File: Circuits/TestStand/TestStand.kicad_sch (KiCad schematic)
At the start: 84 parts, among them J1 Screw_Terminal_01x07, J10 Screw_Terminal_01x03, J11 Screw_Terminal_01x03, J12 Screw_Terminal_01x03, J13 Screw_Terminal_01x03, J14 Screw_Terminal_01x02, J15 Conn_Coaxial, J2 Screw_Terminal_01x07, J3 Screw_Terminal_01x07, J4 Screw_Terminal_01x03, J5 Screw_Terminal_01x03, J6 Screw_Terminal_01x03, J7 Screw_Terminal_01x03, J8 Screw_Terminal_01x03, J9 Screw_Terminal_01x03, Q1 MMBT4403-7-F, Q2 MMBT4403-7-F, Q3 MMBT4403-7-F, U1 HX711, U2 HX711, U3 HX711, U4 Teensy4.1, U5 LP2980IM5X-3.3/NOPB, U6 MAX31855KASA, U7 NRF24L01, U8 LP2980IM5X-3.3/NOPB, Y1 16Mhz

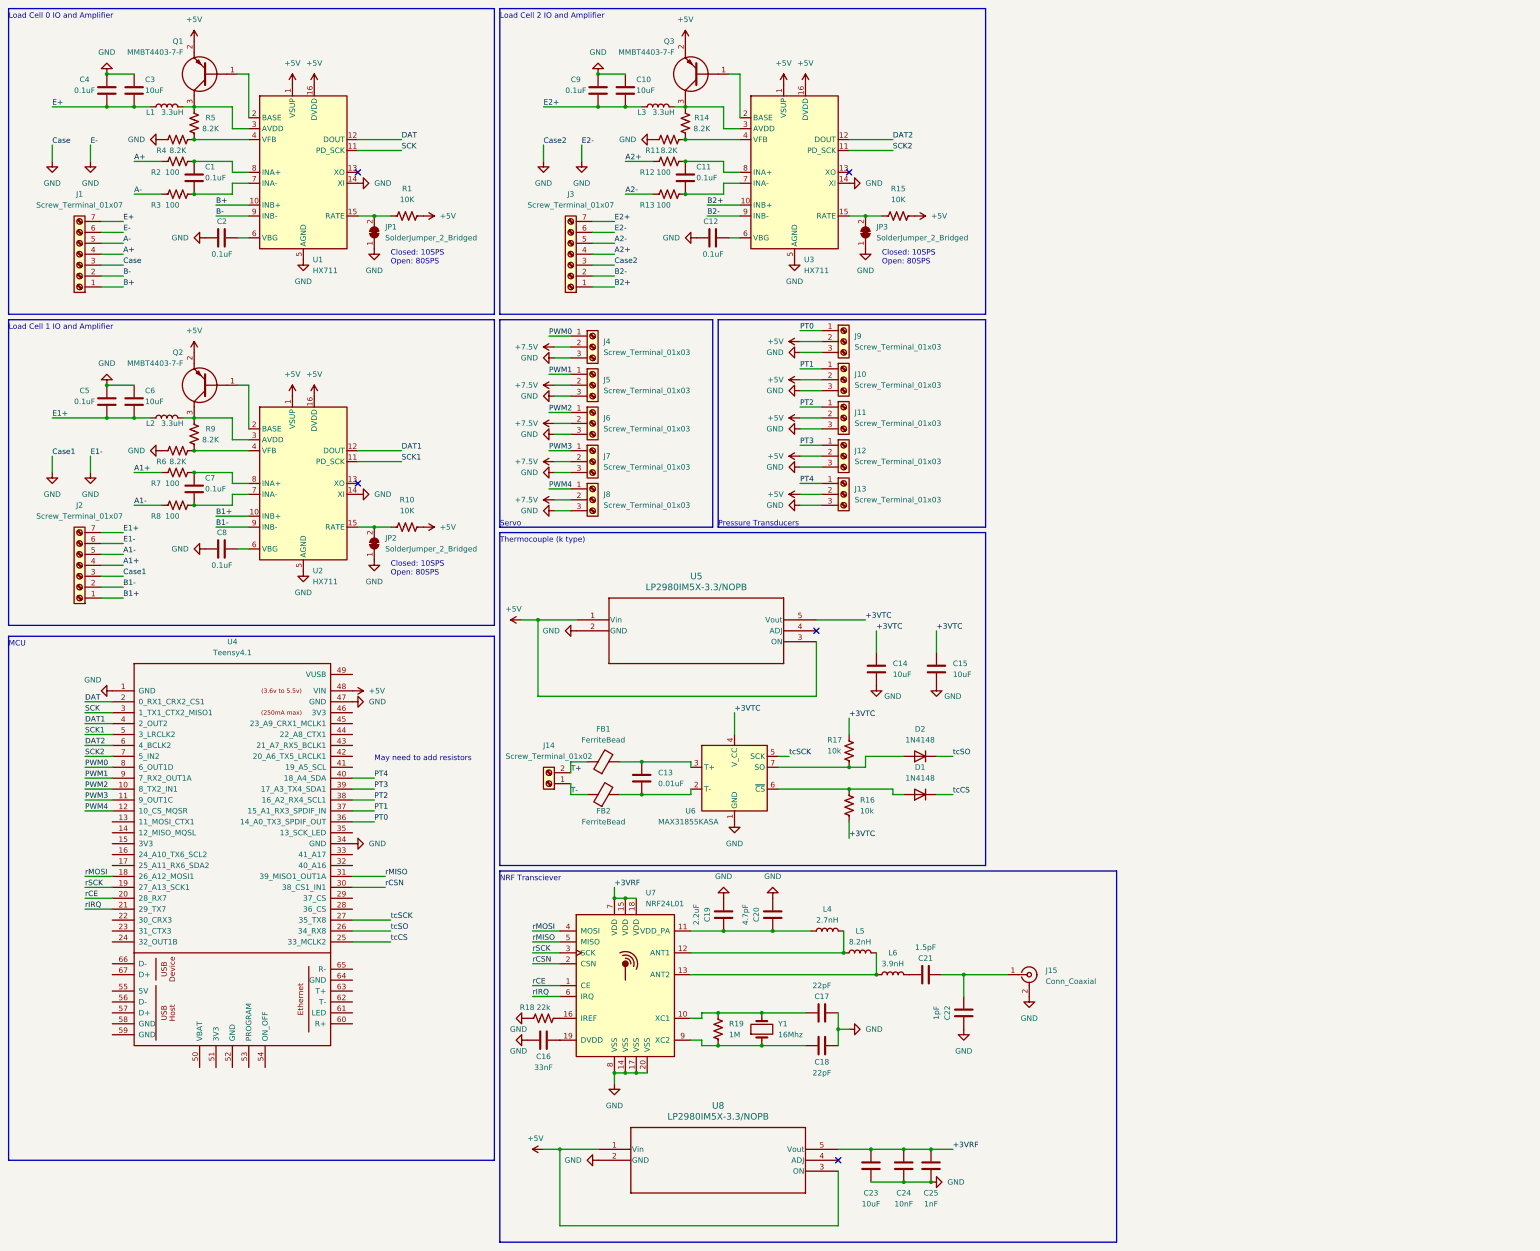
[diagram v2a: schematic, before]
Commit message: added glow plug circuitry to schematic
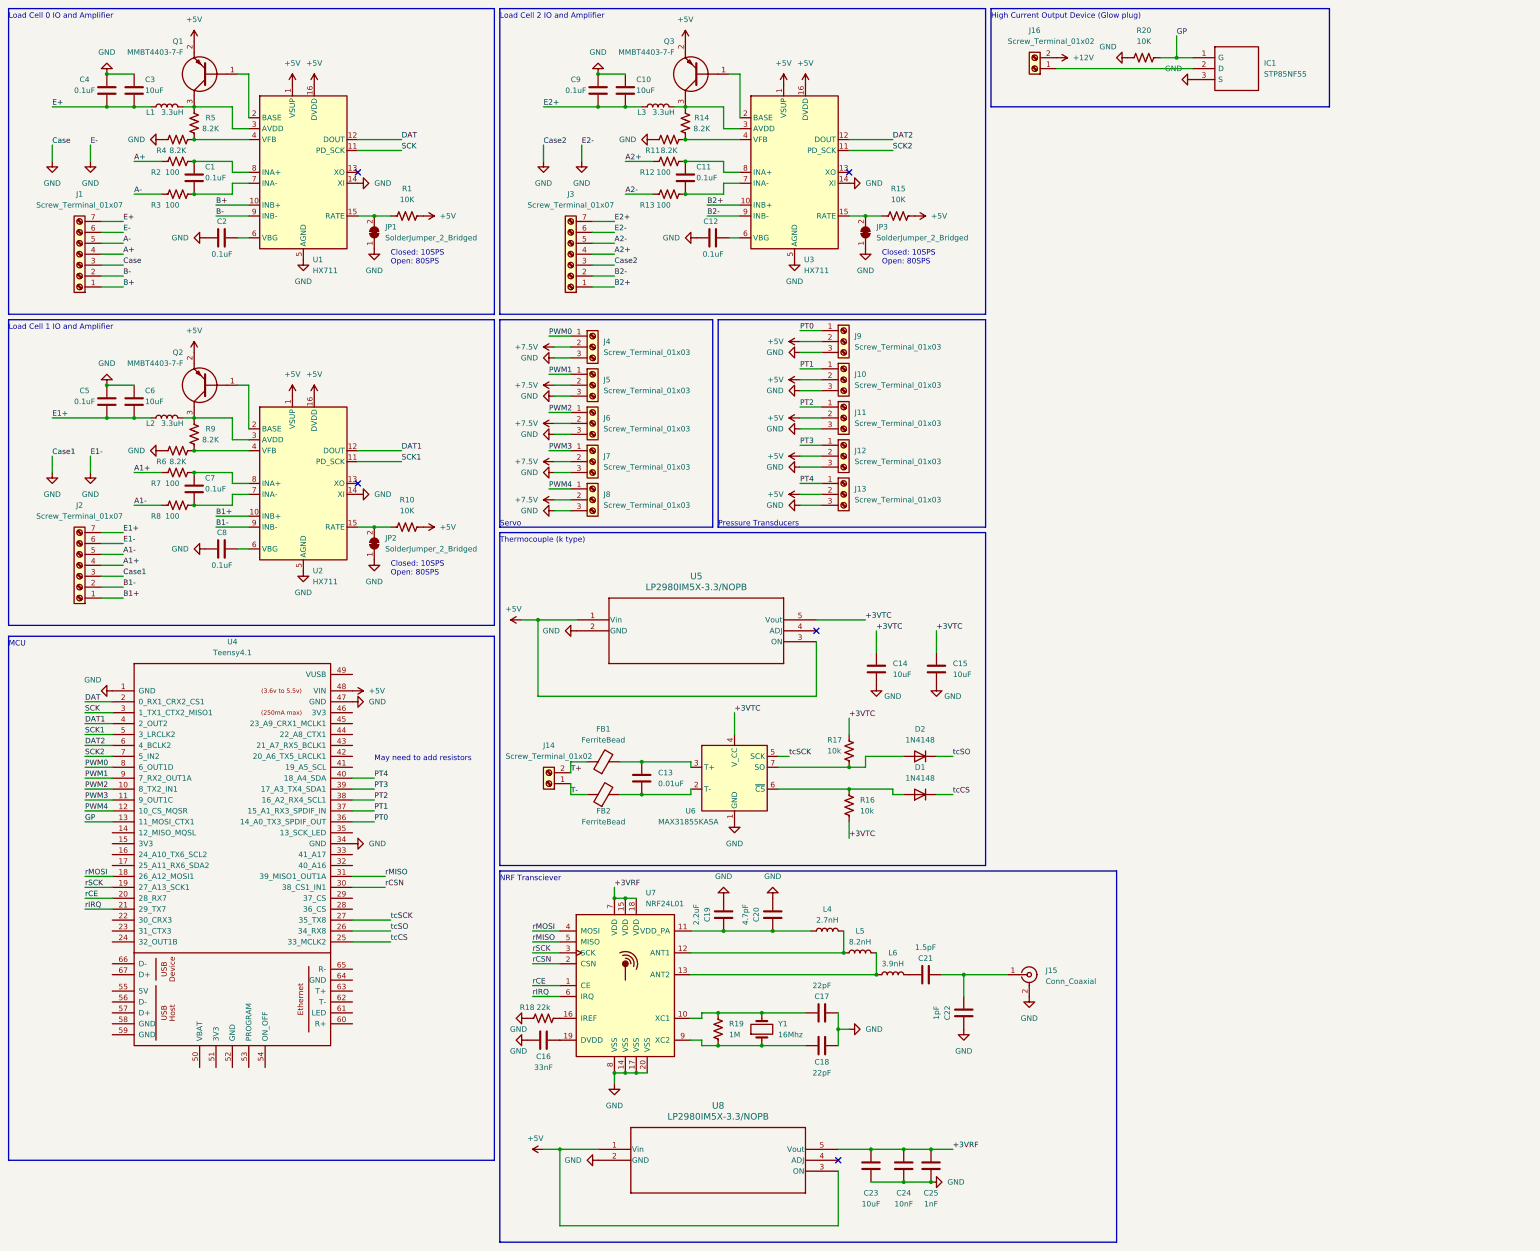
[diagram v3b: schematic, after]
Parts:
- added IC1: STP85NF55, TO255P460X1020X2008-3P, symbol STP85NF55:STP85NF55
- added J16: Screw_Terminal_01x02, Connector_Wago:Wago_734-132_1x02_P3.50mm_Vertical, symbol Connector:Screw_Terminal_01x02
- added R20: 10K, Resistor_SMD:R_0805_2012Metric, symbol Device:R_US
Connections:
- net GND: now also IC1.3 (S), R20.1
- net GP: now reaches U4.13 (11_MOSI_CTX1)
- net GP: now also IC1.1 (G), R20.2
- new net: IC1.2 (D), J16.1 (Pin_1)
- new net +12V: J16.2 (Pin_2)
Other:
- note added: "High Current Output Device (Glow plug)"
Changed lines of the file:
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@@
   (junction (at 59.69 133.35) (diameter 0) (color 0 0 0 0)
   )
+  (junction (at 288.29 29.21) (diameter 0) (color 0 0 0 0)
+  )
   (junction (at 153.67 33.02) (diameter 0) (color 0 0 0 0)
   )
@@
     (stroke (width 0) (type default))
   )
+  (wire (pts (xy 260.35 31.75) (xy 292.1 31.75))
+    (stroke (width 0) (type default))
+  )
+  (wire (pts (xy 284.48 29.21) (xy 288.29 29.21))
+    (stroke (width 0) (type default))
+  )
   (wire (pts (xy 35.56 121.92) (xy 35.56 125.73))
     (stroke (width 0) (type default))
@@
     (stroke (width 0) (type default))
   )
+  (wire (pts (xy 288.29 24.13) (xy 288.29 29.21))
+    (stroke (width 0) (type default))
+  )
   (wire (pts (xy 157.48 265.43) (xy 160.02 265.43))
     (stroke (width 0) (type default))
@@
     (stroke (width 0) (type default))
   )
+  (wire (pts (xy 34.29 207.01) (xy 40.64 207.01))
+    (stroke (width 0) (type default))
+  )
   (wire (pts (xy 69.85 105.41) (xy 72.39 105.41))
     (stroke (width 0) (type default))
@@
     (stroke (width 0) (type default))
   )
+  (wire (pts (xy 288.29 29.21) (xy 292.1 29.21))
+    (stroke (width 0) (type default))
+  )
   (wire (pts (xy 200.66 119.38) (xy 205.74 119.38))
     (stroke (width 0) (type default))
@@
     (fill (type none))
   )
+  (rectangle (start 245.11 17.78) (end 323.85 40.64)
+    (stroke (width 0) (type default))
+    (fill (type none))
+  )
   (rectangle (start 130.81 218.44) (end 274.32 304.8)
     (stroke (width 0) (type default))
@@
     (effects (font (size 1.27 1.27)) (justify left bottom))
   )
+  (text "High Current Output Device (Glow plug)\n" (at 245.11 20.32 0)
+    (effects (font (size 1.27 1.27)) (justify left bottom))
+  )
   (text "Closed: 10SPS\nOpen: 80SPS" (at 105.41 149.86 0)
     (effects (font (size 1.27 1.27)) (justify left bottom))
@@
     (effects (font (size 1.27 1.27)) (justify left bottom))
   )
+  (label "GP" (at 34.29 207.01 0) (fields_autoplaced)
+    (effects (font (size 1.27 1.27)) (justify left bottom))
+  )
   (label "rCSN" (at 138.43 240.03 0) (fields_autoplaced)
     (effects (font (size 1.27 1.27)) (justify left bottom))
@@
     (effects (font (size 1.27 1.27)) (justify left bottom))
   )
+  (label "GP" (at 288.29 24.13 0) (fields_autoplaced)
+    (effects (font (size 1.27 1.27)) (justify left bottom))
+  )
   (label "A1-" (at 45.72 133.35 0) (fields_autoplaced)
     (effects (font (size 1.27 1.27)) (justify left bottom))
@@
     )
   )
+  (symbol (lib_id "power:GND") (at 292.1 34.29 270) (unit 1)
+    (in_bom yes) (on_board yes) (dnp no)
+    (property "Reference" "#PWR079" (at 285.75 34.29 0)
+      (effects (font (size 1.27 1.27)) hide)
+    )
+    (property "Value" "GND" (at 289.56 31.75 90)
+      (effects (font (size 1.27 1.27)) (justify right))
+    )
+    (property "Footprint" "" (at 292.1 34.29 0)
+      (effects (font (size 1.27 1.27)) hide)
+    )
+    (property "Datasheet" "" (at 292.1 34.29 0)
+      (effects (font (size 1.27 1.27)) hide)
+    )
+    (pin "1")
+    (instances
+      (project "TestStand"
+        (path "/685411e9-e044-4af3-ae59-8bb36f8f4098"
+          (reference "#PWR079") (unit 1)
+        )
+      )
+    )
+  )
   (symbol (lib_id "power:GND") (at 35.56 53.34 0) (unit 1)
     (in_bom yes) (on_board yes) (dnp no) (fields_autoplaced)
@@
     )
   )
+  (symbol (lib_id "power:+12V") (at 260.35 29.21 270) (unit 1)
+    (in_bom yes) (on_board yes) (dnp no) (fields_autoplaced)
+    (property "Reference" "#PWR077" (at 256.54 29.21 0)
+      (effects (font (size 1.27 1.27)) hide)
+    )
+    (property "Value" "+12V" (at 264.16 29.21 90)
+      (effects (font (size 1.27 1.27)) (justify left))
+    )
+    (property "Footprint" "" (at 260.35 29.21 0)
+      (effects (font (size 1.27 1.27)) hide)
+    )
+    (property "Datasheet" "" (at 260.35 29.21 0)
+      (effects (font (size 1.27 1.27)) hide)
+    )
+    (pin "1")
+    (instances
+      (project "TestStand"
+        (path "/685411e9-e044-4af3-ae59-8bb36f8f4098"
+          (reference "#PWR077") (unit 1)
+        )
+      )
+    )
+  )
   (symbol (lib_id "power:+5V") (at 82.55 107.95 0) (unit 1)
     (in_bom yes) (on_board yes) (dnp no) (fields_autoplaced)
@@
     )
   )
+  (symbol (lib_id "STP85NF55:STP85NF55") (at 292.1 29.21 0) (unit 1)
+    (in_bom yes) (on_board yes) (dnp no) (fields_autoplaced)
+    (property "Reference" "IC1" (at 308.61 30.48 0)
+      (effects (font (size 1.27 1.27)) (justify left))
+    )
+    (property "Value" "STP85NF55" (at 308.61 33.02 0)
+      (effects (font (size 1.27 1.27)) (justify left))
+    )
+    (property "Footprint" "TO255P460X1020X2008-3P" (at 308.61 26.67 0)
+      (effects (font (size 1.27 1.27)) (justify left) hide)
+    )
+    (property "Datasheet" "https://www.st.com/resource/en/datasheet/stb85nf55t4.pdf" (at 308.61 29.21 0)
+      (effects (font (size 1.27 1.27)) (justify left) hide)
+    )
+    (property "Description" "Automotive-grade N-channel 55 V, 0.0062 Ohm typ., 42 A, STripFET(TM) II Power MOSFET in TO-220 package" (at 308.61 31.75 0)
+      (effects (font (size 1.27 1.27)) (justify left) hide)
+    )
+    (property "Height" "4.6" (at 308.61 34.29 0)
+      (effects (font (size 1.27 1.27)) (justify left) hide)
+    )
+    (property "Mouser Part Number" "511-STP85NF55" (at 308.61 36.83 0)
+      (effects (font (size 1.27 1.27)) (justify left) hide)
+    )
+    (property "Mouser Price/Stock" "https://www.mouser.co.uk/ProductDetail/STMicroelectronics/STP85NF55?qs=mdiO5HdF0KgIATm5G3vEuw%3D%3D" (at 308.61 39.37 0)
+      (effects (font (size 1.27 1.27)) (justify left) hide)
+    )
+    (property "Manufacturer_Name" "STMicroelectronics" (at 308.61 41.91 0)
+      (effects (font (size 1.27 1.27)) (justify left) hide)
+    )
+    (property "Manufacturer_Part_Number" "STP85NF55" (at 308.61 44.45 0)
+      (effects (font (size 1.27 1.27)) (justify left) hide)
+    )
+    (pin "3")
+    (pin "1")
+    (pin "2")
+    (instances
+      (project "TestStand"
+        (path "/685411e9-e044-4af3-ae59-8bb36f8f4098"
+          (reference "IC1") (unit 1)
+        )
+      )
+    )
+  )
   (symbol (lib_id "Device:C") (at 205.74 251.46 90) (unit 1)
     (in_bom yes) (on_board yes) (dnp no)
@@
     )
   )
+  (symbol (lib_id "Connector:Screw_Terminal_01x02") (at 255.27 31.75 180) (unit 1)
+    (in_bom yes) (on_board yes) (dnp no)
+    (property "Reference" "J16" (at 255.27 22.86 0)
+      (effects (font (size 1.27 1.27)))
+    )
+    (property "Value" "Screw_Terminal_01x02" (at 259.08 25.4 0)
+      (effects (font (size 1.27 1.27)))
+    )
+    (property "Footprint" "Connector_Wago:Wago_734-132_1x02_P3.50mm_Vertical" (at 255.27 31.75 0)
+      (effects (font (size 1.27 1.27)) hide)
+    )
+    (property "Datasheet" "~" (at 255.27 31.75 0)
+      (effects (font (size 1.27 1.27)) hide)
+    )
+    (pin "1")
+    (pin "2")
+    (instances
+      (project "TestStand"
+        (path "/685411e9-e044-4af3-ae59-8bb36f8f4098"
+          (reference "J16") (unit 1)
+        )
+      )
+    )
+  )
   (symbol (lib_id "Device:L") (at 53.34 40.64 90) (unit 1)
     (in_bom yes) (on_board yes) (dnp no)
@@
     )
   )
+  (symbol (lib_id "Device:R_US") (at 280.67 29.21 90) (unit 1)
+    (in_bom yes) (on_board yes) (dnp no) (fields_autoplaced)
+    (property "Reference" "R20" (at 280.67 22.86 90)
+      (effects (font (size 1.27 1.27)))
+    )
+    (property "Value" "10K" (at 280.67 25.4 90)
+      (effects (font (size 1.27 1.27)))
+    )
+    (property "Footprint" "Resistor_SMD:R_0805_2012Metric" (at 280.924 28.194 90)
+      (effects (font (size 1.27 1.27)) hide)
+    )
+    (property "Datasheet" "~" (at 280.67 29.21 0)
+      (effects (font (size 1.27 1.27)) hide)
+    )
+    (pin "2")
+    (pin "1")
+    (instances
+      (project "TestStand"
+        (path "/685411e9-e044-4af3-ae59-8bb36f8f4098"
+          (reference "R20") (unit 1)
+        )
+      )
+    )
+  )
   (symbol (lib_id "Device:R_US") (at 59.69 44.45 0) (unit 1)
     (in_bom yes) (on_board yes) (dnp no)
@@
         )
       )
+    )
+  )
+  (symbol (lib_id "power:GND") (at 276.86 29.21 270) (unit 1)
+    (in_bom yes) (on_board yes) (dnp no)
+    (property "Reference" "#PWR078" (at 270.51 29.21 0)
+      (effects (font (size 1.27 1.27)) hide)
+    )
+    (property "Value" "GND" (at 274.32 26.67 90)
+      (effects (font (size 1.27 1.27)) (justify right))
+    )
+    (property "Footprint" "" (at 276.86 29.21 0)
+      (effects (font (size 1.27 1.27)) hide)
+    )
+    (property "Datasheet" "" (at 276.86 29.21 0)
+      (effects (font (size 1.27 1.27)) hide)
+    )
+    (pin "1")
+    (instances
+      (project "TestStand"
+        (path "/685411e9-e044-4af3-ae59-8bb36f8f4098"
+          (reference "#PWR078") (unit 1)
+        )
+      )
